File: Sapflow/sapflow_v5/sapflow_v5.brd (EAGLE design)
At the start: 42.5 x 53.3 mm, 47 parts, among them Q1 NMOS, Q4 NMOS, Q5 NMOS, U1 MAXIM_MAX5033BASA+MAXIM_MAX50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

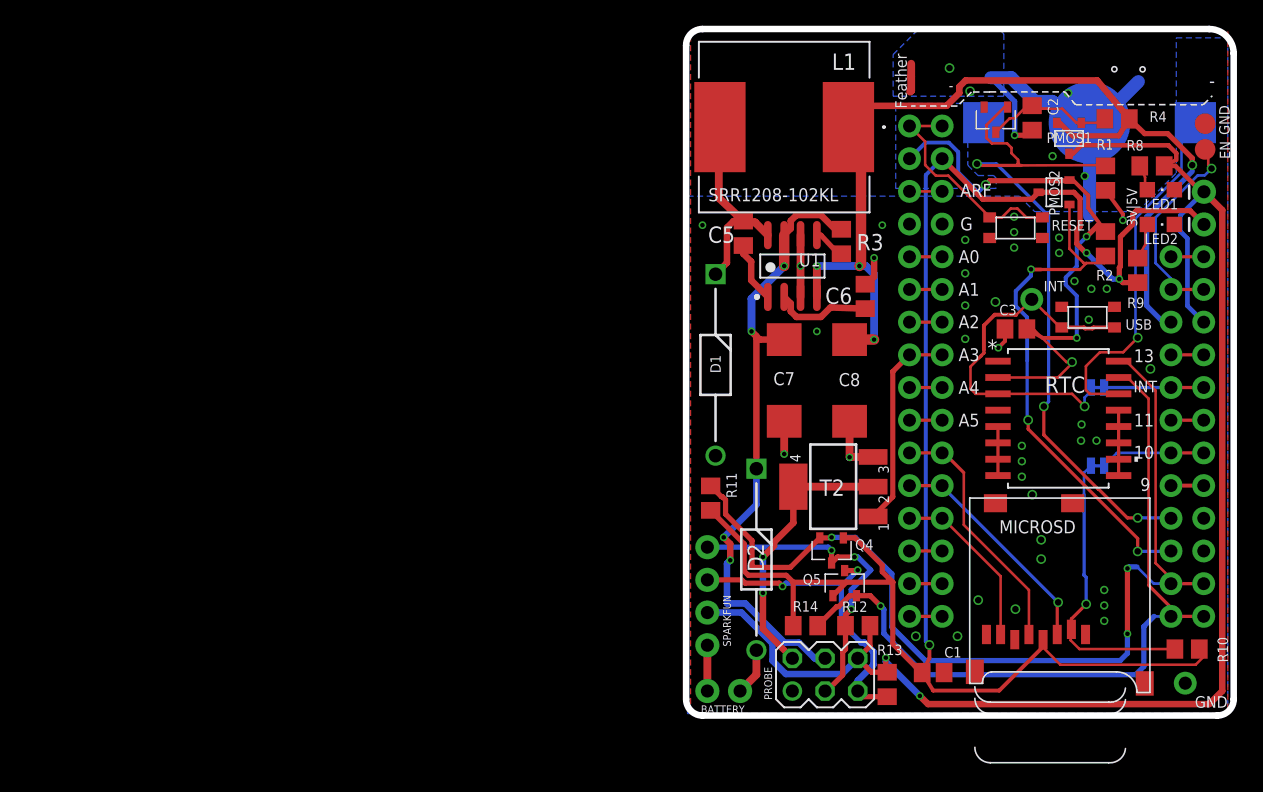
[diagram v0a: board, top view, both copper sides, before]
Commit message: changed to v5 of sapflow wing
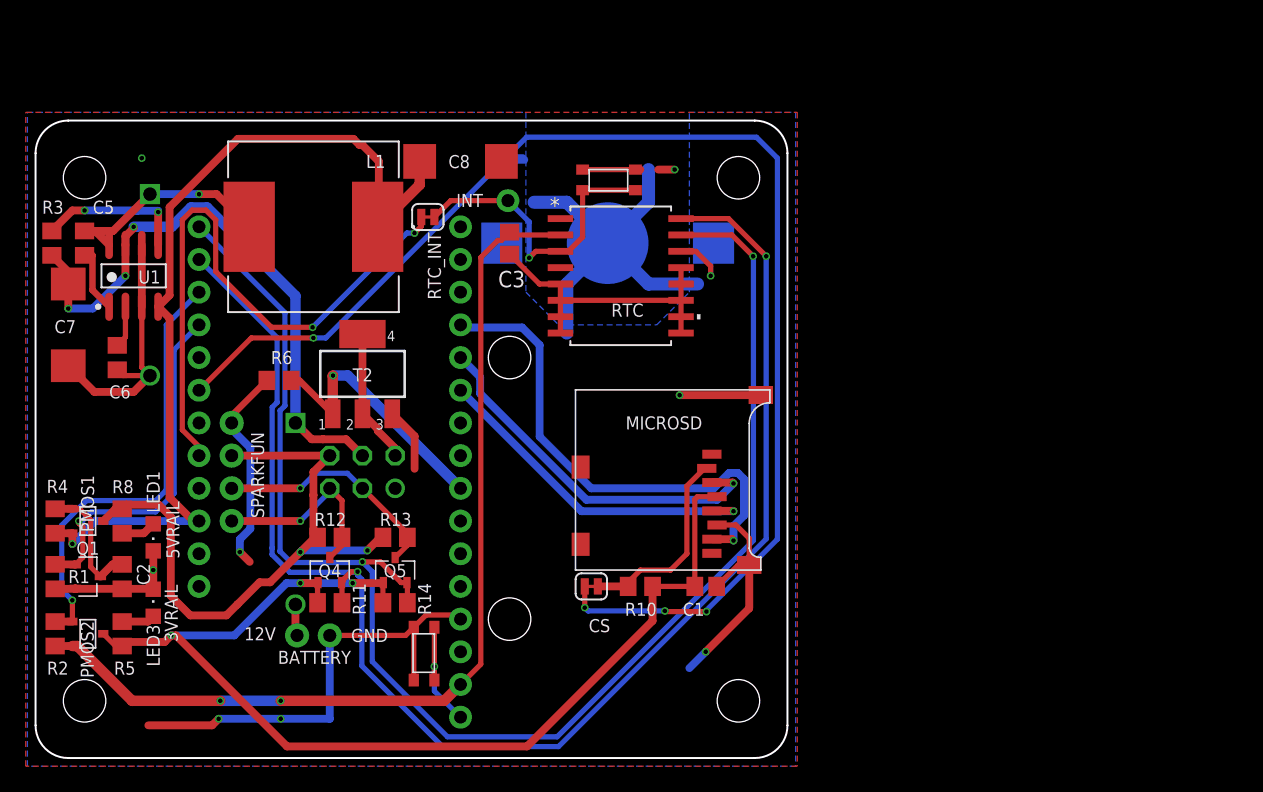
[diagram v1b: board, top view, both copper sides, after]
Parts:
- removed 3V|5V: (no value), SparkFun-Connectors:1X02_NO_SILK
- removed JP1: (no value), adafruit:1X01-CLEANBIG
- removed LED2: RED, adafruit:CHIPLED_0805
- removed MS1: FEATHERWING, powerboard:FEATHERWING
- removed R9: 910, rcl:R0805
- removed TP1, TP2: TPTP16R, testpad:TP16R
- added H2, H4, H5, H6, H7, H8: STAND-OFF, SparkFun-Hardware:STAND-OFF
- added LED3: RED, adafruit:CHIPLED_0805
- added LOGO1: OSHW-LOGOM, SparkFun-Aesthetics:OSHW-LOGO-M
- added R5: 910, rcl:R0805
- added R6: 40k, rcl:R0805
- MICROSD: device adafruit:MICROSD -> adafruit_improved:MICROSD
- moved R4 88.2 mm to (-57.3, 18.3), turned to 270 degrees
- moved R1 87.3 mm to (-57.3, 14.0)
- moved R2 87.1 mm to (-57.3, 9.53), turned to 270 degrees
- moved R8 84.6 mm to (-52.1, 18.3), turned to 90 degrees
- moved LED1 82.8 mm to (-49.7, 17.0), turned to 180 degrees
- moved PMOS2 82.5 mm to (-54.7, 9.53), turned to 0 degrees
- moved PMOS1 81.8 mm to (-54.7, 18.3), turned to 0 degrees
- moved C2 79.2 mm to (-52.1, 14.0)
- moved Q1 79.0 mm to (-54.7, 14.0), turned to 0 degrees
- moved MS2 67.0 mm to (-24.5, -3.30), turned to 90 degrees
- moved R3 61.3 mm to (-57.5, 39.9), turned to 270 degrees
- moved C6 58.3 mm to (-52.5, 31.0), turned to 270 degrees
- moved C7 55.8 mm to (-56.3, 33.5)
- moved RTC_INT 53.7 mm to (-28.3, 41.9), flipped to the top
- moved U$1 53.6 mm to (-27.8, 10.0), turned to 270 degrees
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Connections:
- net +12V renamed 12V
- net +3V3 renamed 3V3
- net 5VUSB renamed 5V
- net N$1 renamed 5V_EN
- net N$3 renamed 3V_EN
- removed net A3: MS1.8, MS2.8, T2.1
- removed net N$13: LED2.A, R9.1
- removed net N$7: MS1.20
- removed net N$8: MS1.19
- removed net RESET: MS1.1, MS2.1, U$1.3, U$1.4
- new net HTR_EN: MS2.8, R6.2, T2.1
- new net N$1: MS2.1, U$1.3, U$1.4
- new net N$5: LED3.A, R5.1
- net 0RX: no longer MS1.14
- net 11: no longer MS1.23
- net 13: no longer MS1.25
- net 1TX: no longer MS1.15
- net 3VRAIL: now also R5.2; no longer 3V|5V.1, MS1.2, R9.2
- net 5VRAIL: no longer 3V|5V.2, MS1.26
- net 9: no longer MS1.21
- net A0: no longer MS1.5
- net A1: no longer MS1.6
- net A2: no longer MS1.7
- net A4: no longer MS1.9
- net A5: no longer MS1.10
- net ARF: no longer MS1.3
- net CLK: no longer MS1.11
- net DFU: no longer MS1.16
- net DI: no longer MS1.12
- net DO: no longer MS1.13
- net EN: no longer MS1.27, TP1.TP
- net GND: now also LED3.C, R6.1; no longer JP1.1, LED2.C, MS1.4, TP2.TP
- net N$11: no longer MS1.22
- net N$14: no longer MS1.24
- net SCL: no longer MS1.18
- net SCL_5: now also PROBE.5; no longer PROBE.3
- net SDA: no longer MS1.17
- net SDA_5: now also PROBE.3; no longer PROBE.5
- net VBATT: no longer MS1.28
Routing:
- net GND: track 61.8 -> 173.8 mm, vias 43 -> 8
- net N$11: track 8.16 -> 102.5 mm, vias 0 -> 4
- net 5VRAIL: track 115.4 -> 48.4 mm
- net SDA: track 58.9 -> 115.4 mm, vias 1 -> 2
- net 3VRAIL: track 137.4 -> 88.3 mm
- net N$14: track 7.74 -> 47.8 mm, vias 0 -> 2
- net SCL: track 76.8 -> 114.0 mm, vias 3 -> 2
- net 3V3: track 46.9 -> 74.7 mm, vias 4 -> 2
- net 5V_EN: track 54.9 -> 27.5 mm, vias 3 -> 1
- net DO: track 13.5 -> 39.0 mm, vias 0 -> 1
- net N$2: track 28.2 -> 6.16 mm
- net HTR_EN: track 0.00 -> 20.8 mm, vias 0 -> 1
- net RESET: track 17.5 -> 0.00 mm
- net EN: track 16.3 -> 0.00 mm, vias 1 -> 0
- net A3: track 16.3 -> 0.00 mm
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- removed copper zone on layer 16, net 3V3
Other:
- board size 42.5 x 53.3 mm -> 58.4 x 49.5 mm
- board text added: "12V"
- board text added: "12_V"
- board text added: "3VRAIL"
- board text added: "5VRAIL"
- board text added: "5V_RAIL"
- board text added: "April 2020"
- board text added: "HEATER-"
- board text added: "Josh Barksdale"
- board text added: "SCL_5"
- board text added: "SDA_5"
- board text added: "Sapflow Wing v5"
- board text removed: "+IN"
- board text removed: "-"
- board text removed: "10"
- board text removed: "11"
- board text removed: "13"
- board text removed: "3V"
- board text removed: "5V"
- board text removed: "9"
- board text removed: "A0"
- board text removed: "A1"
- board text removed: "A2"
- board text removed: "A3"
- board text removed: "A4"
- board text removed: "A5"
- board text removed: "ARF"
- board text removed: "BAT"
- board text removed: "BAT+"
- board text removed: "BAT-"
- board text removed: "Control"
- board text removed: "DFU"
- board text removed: "EN"
- board text removed: "Feather"
- board text removed: "G"
- board text removed: "HTR+"
- board text removed: "HTR-"
- board text removed: "INT"
- board text removed: "Josh Barksdale & Bao Nguyen"
- board text removed: "MI"
- board text removed: "MO"
- board text removed: "March 2020"
- board text removed: "Optional I2C Pull Up"
- board text removed: "RESET"
- board text removed: "RTC"
- board text removed: "Rx"
- board text removed: "SCK"
- board text removed: "SCL"
- board text removed: "SDA"
- board text removed: "SDCS"
- board text removed: "Sapflow Wing v.4"
- board text removed: "Tx"
- board text removed: "USB"
